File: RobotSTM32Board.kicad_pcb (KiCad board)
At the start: 2 copper layers, 70 x 82.5 mm, 74 parts, among them IC1 TB6612FNG, IC2 TB6612FNG, J1 MotorA, J10 Qwiik1, J11 Qwiik2, J12 Qwiik3, J13 Qwiik4, J14 Qwiik5, J2 MotorB, J3 MotorC, J4 MotorD, J5 EncoderA, J6 EncoderB, J7 EncoderC, J8 EncoderD, J9 ESTOP, Q1 NPN, Q2 NMOS_Substrate, Q3 NMOS_Substrate, U1 NUCLEO-F411RE, U3 TPS564252DRLR, U4 TPS51386RJNR, U5 LM27403SQ/NOPB

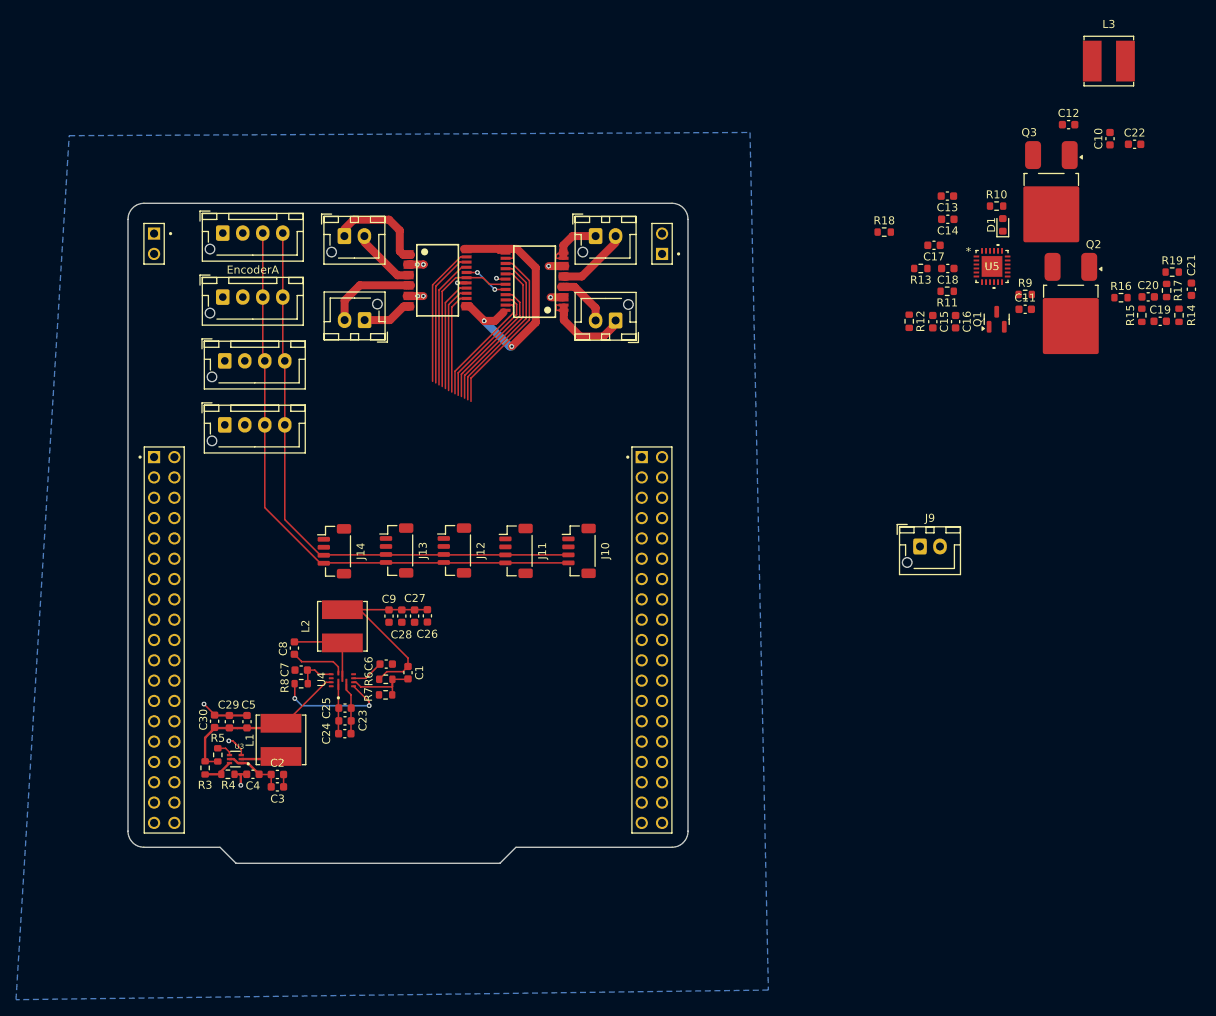
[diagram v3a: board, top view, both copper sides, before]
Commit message: pcb routed
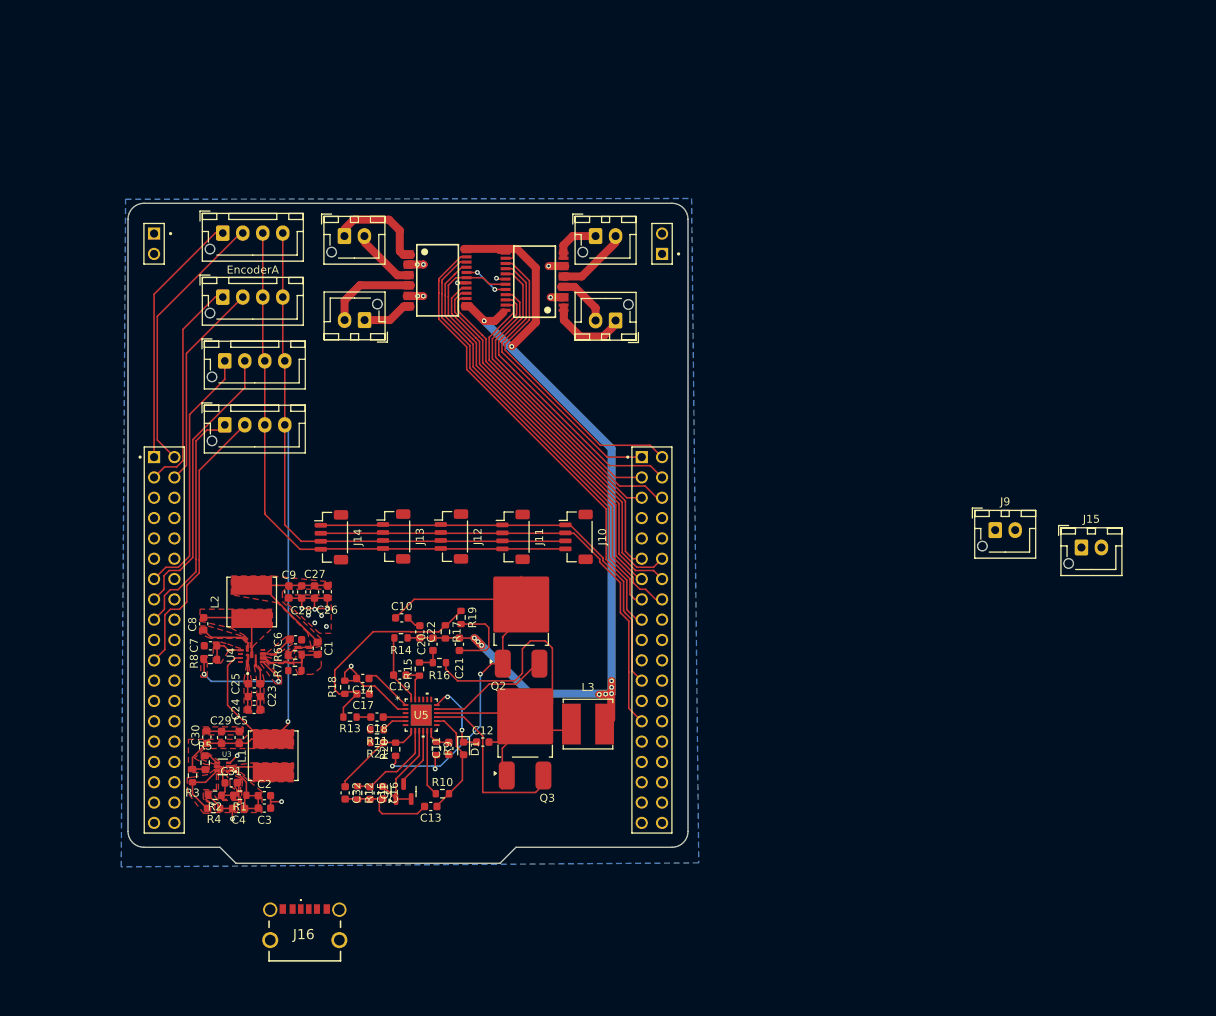
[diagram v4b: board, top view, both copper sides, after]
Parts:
- added ?: , , B.Cu at (145.2, 116.2)
- added C31: 10nF, Capacitor_SMD:C_0603_1608Metric, F.Cu at (121.4, 124.7)
- added C32: 10nF, Capacitor_SMD:C_0603_1608Metric, F.Cu at (135.6, 125.9)
- added J15: DCIn, Connector_JST:JST_XH_B2B-XH-AM_1x02_P2.50mm_Vertical, F.Cu at (227.7, 95.3)
- added J16: UJC-H-G-SMT-2-P6-TR, USBCC:UJCHGSMT2P6TR, F.Cu at (130.6, 143.5)
- added R1: 47k, Resistor_SMD:R_0603_1608Metric, F.Cu at (122.5, 126.2)
- added R2: 20k, Resistor_SMD:R_0603_1608Metric, F.Cu at (119.4, 126.2)
- added R20: 47k, Resistor_SMD:R_0603_1608Metric, F.Cu at (141.9, 120.5)
- added R21: 20k, Resistor_SMD:R_0603_1608Metric, F.Cu at (139.6, 119.7)
- moved C22 108.2 mm to (145.0, 105.8), turned to -90 degrees
- moved C10 106.9 mm to (142.7, 104.1), turned to 0 degrees
- moved C12 106.4 mm to (152.8, 119.6)
- moved L3 105.4 mm to (166.0, 117.3)
- moved R14 105.3 mm to (142.6, 106.6), turned to 0 degrees
- moved C19 104.8 mm to (142.5, 111.2), turned to 180 degrees
- moved C21 101.7 mm to (149.9, 107.4), turned to 90 degrees
- moved R10 101.0 mm to (147.8, 126.0)
- moved R15 100.5 mm to (144.9, 110.5)
- moved C13 100.0 mm to (146.3, 127.7)
- moved R17 99.7 mm to (148.2, 105.8)
- moved C20 99.4 mm to (146.6, 107.4), turned to 90 degrees
- moved R19 98.8 mm to (150.1, 104.0), turned to -90 degrees
- moved R16 96.6 mm to (147.4, 109.7)
- moved Q1 94.8 mm to (142.9, 125.8)
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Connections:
- U1 pad CN10_1: unconnected-(U1B-PC9-PadCN10_1) -> MotorDCW
- U1 pad CN10_11: unconnected-(U1B-PA5-PadCN10_11) -> MotorPWMB
- U1 pad CN10_12: unconnected-(U1B-PA12-PadCN10_12) -> MotorBCW
- U1 pad CN10_13: unconnected-(U1B-PA6-PadCN10_13) -> ESTOP
- U1 pad CN10_14: unconnected-(U1B-PA11-PadCN10_14) -> MotorBCCW
- U1 pad CN10_15: unconnected-(U1B-PA7-PadCN10_15) -> MotorACCW
- U1 pad CN10_16: unconnected-(U1B-PB12-PadCN10_16) -> MotorACW
- U1 pad CN10_17: unconnected-(U1B-PB6-PadCN10_17) -> MotorPWMA
- U1 pad CN10_2: unconnected-(U1B-PC8-PadCN10_2) -> MotorPWMD
- U1 pad CN10_23: unconnected-(U1B-PA8-PadCN10_23) -> SCL
- U1 pad CN10_27: unconnected-(U1B-PB4-PadCN10_27) -> SDA
- U1 pad CN10_3: unconnected-(U1B-PB8-PadCN10_3) -> MotorCCW
- U1 pad CN10_4: unconnected-(U1B-PC6-PadCN10_4) -> MotorDCCW
- U1 pad CN10_5: unconnected-(U1B-PB9-PadCN10_5) -> MotorPWMC
- U1 pad CN10_6: unconnected-(U1B-PC5-PadCN10_6) -> MotorCCCW
- U1 pad CN10_9: unconnected-(U1B-GND_9-PadCN10_9) -> GND
- U1 pad CN7_1: MotorPWMA -> EncoderA1
- U1 pad CN7_13: MotorBCW -> EncoderC1
- U1 pad CN7_15: unconnected-(U1A-PA14-PadCN7_15) -> EncoderC2
- U1 pad CN7_17: unconnected-(U1A-PA15-PadCN7_17) -> EncoderD1
- U1 pad CN7_19: unconnected-(U1A-GND_19-PadCN7_19) -> GND
- U1 pad CN7_2: MotorACCW -> EncoderA2
- U1 pad CN7_21: unconnected-(U1A-PB7-PadCN7_21) -> EncoderD2
- U1 pad CN7_22: unconnected-(U1A-GND_22-PadCN7_22) -> GND
- U1 pad CN7_3: MotorACW -> EncoderB1
- U1 pad CN7_4: MotorBCCW -> EncoderB2
- U1 pad CN7_8: unconnected-(U1A-GND_8-PadCN7_8) -> GND
- U3 pad 5: Vin -> Net-(U3-EN)
- U5 pad 6: unconnected-(U5-SYNC-Pad6) -> GND
- U5 pad 7: unconnected-(U5-UVLO/EN-Pad7) -> Net-(U5-UVLO/EN)
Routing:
- net 6V: track 37.4 -> 123.3 mm, vias 2 -> 10
- net Net-(Q2-Bulk): track 0.00 -> 63.6 mm
- net SDA: track 0.00 -> 58.7 mm
- net Vin: track 13.7 -> 70.8 mm, vias 0 -> 3
- net SCL: track 0.00 -> 54.4 mm
- net GND: track 113.3 -> 160.3 mm, vias 11 -> 19
- net 3V3: track 102.5 -> 147.4 mm, vias 2 -> 3
- net MotorPWMA: track 17.7 -> 58.1 mm
- net MotorACW: track 16.5 -> 55.1 mm
- net MotorACCW: track 17.2 -> 54.8 mm
- net MotorBCCW: track 14.1 -> 49.7 mm
- net EncoderC2: track 0.00 -> 35.3 mm
- net EncoderD2: track 0.00 -> 34.8 mm
- net MotorBCW: track 13.6 -> 48.3 mm
- net ESTOP: track 20.9 -> 54.8 mm
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- added copper zone on F.Cu, net 3V3
- added copper zone on F.Cu, net 5V
- added copper zone on F.Cu, net GND
- added copper zone on F.Cu, net Net-(U3-EN)
- added copper zone on F.Cu, net Net-(U3-FB)
- added copper zone on F.Cu, net Net-(U3-PG)
- added copper zone on F.Cu, net Net-(U3-SW)
- added copper zone on F.Cu, net Net-(U4-FB)
- added copper zone on F.Cu, net Net-(U4-PG)
- added copper zone on F.Cu, net Net-(U4-SS)
- added copper zone on F.Cu, net Net-(U4-SW)
- added copper zone on F.Cu, net Net-(U4-VBST)
- added copper zone on F.Cu, net Net-(U4-VCC)
- added copper zone on F.Cu, net Vin

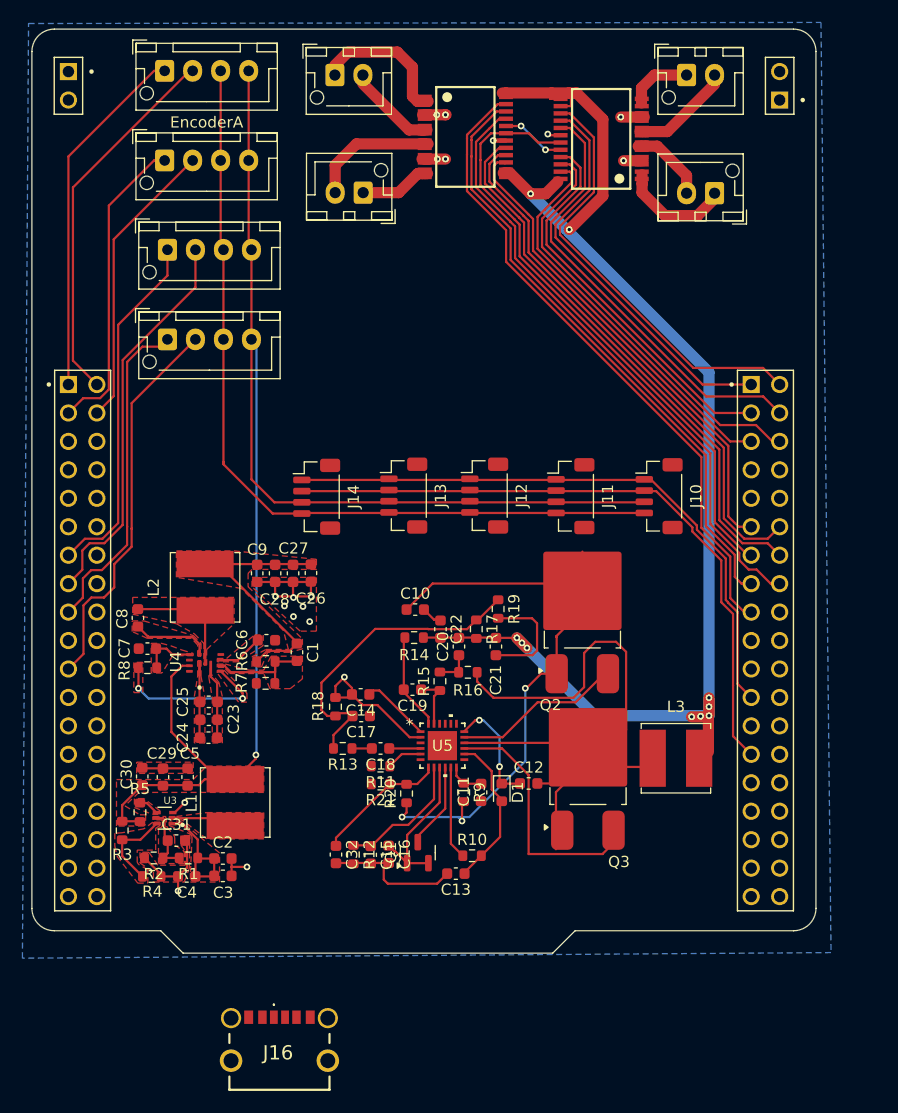
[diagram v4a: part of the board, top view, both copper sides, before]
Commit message: correcting DRC's
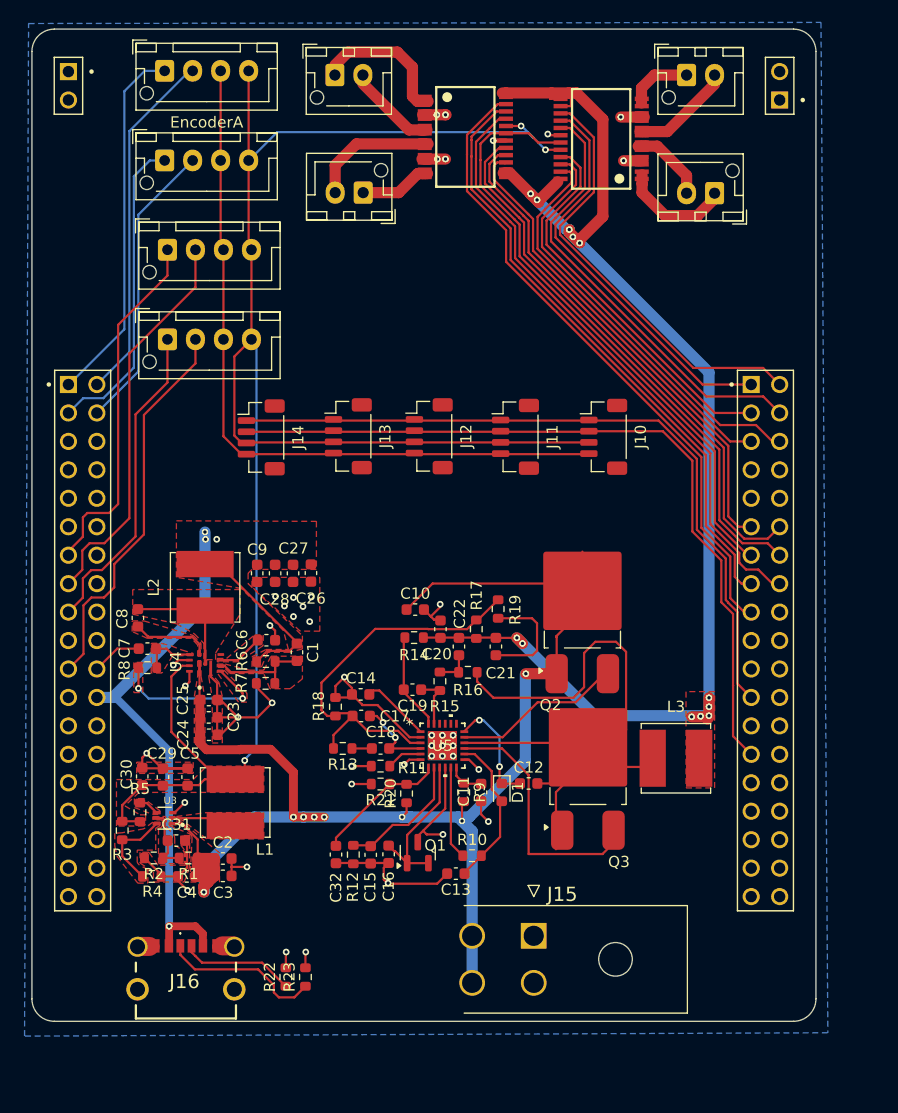
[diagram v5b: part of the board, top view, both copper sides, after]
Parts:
- added J15: 39-30-0040, KiCad:39-30-Y040, F.Cu at (153.3, 133.2)
- added R22: 20k, Resistor_SMD:R_0603_1608Metric, F.Cu at (131.2, 136.9)
- added R23: 20k, Resistor_SMD:R_0603_1608Metric, F.Cu at (132.9, 136.9)
- moved J16 10.5 mm to (122.2, 137.1)
- moved J12 7.25 mm to (144.0, 88.6)
- moved J14 7.25 mm to (129.0, 88.7)
- moved J13 7.25 mm to (136.8, 88.6)
- moved J10 7.25 mm to (159.6, 88.7)
- moved J11 7.25 mm to (151.7, 88.7)
- moved C24 0.27 mm to (124.3, 115.2)
- moved C23 0.21 mm to (124.3, 113.7)
- moved C25 0.16 mm to (124.3, 112.2)
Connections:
- J16 pad 1: unconnected-(J16-MH1-Pad1) -> GND
- J16 pad 2: unconnected-(J16-MH2-Pad2) -> GND
- J16 pad 3: unconnected-(J16-MH3-Pad3) -> GND
- J16 pad 4: unconnected-(J16-MH4-Pad4) -> GND
- J16 pad A12: unconnected-(J16-GND_1-PadA12) -> GND
- J16 pad A5: unconnected-(J16-CC1-PadA5) -> Net-(J16-CC1)
- J16 pad A9: unconnected-(J16-VBUS_1-PadA9) -> 5V
- J16 pad B12: unconnected-(J16-GND_2-PadB12) -> GND
- J16 pad B5: unconnected-(J16-CC2-PadB5) -> Net-(J16-CC2)
- J16 pad B9: unconnected-(J16-VBUS_2-PadB9) -> 5V
- U1 pad CN7_24: unconnected-(U1A-VIN-PadCN7_24) -> 5V
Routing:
- net Vin: track 70.8 -> 136.0 mm, vias 3 -> 8
- net 5V: track 25.0 -> 65.5 mm, vias 0 -> 4
- net GND: track 160.3 -> 186.5 mm, vias 19 -> 44
- net 3V3: track 147.4 -> 166.9 mm
- net Net-(J16-CC1): track 0.00 -> 14.3 mm
- net SDA: track 58.7 -> 69.3 mm
- net SCL: track 54.4 -> 64.9 mm
- net Net-(J16-CC2): track 0.00 -> 10.2 mm
- net Net-(U5-FB): track 28.1 -> 35.2 mm
- net Net-(U5-COMP): track 2.80 -> 7.22 mm, vias 0 -> 2
- net EncoderA2: track 33.5 -> 31.7 mm
- net EncoderD1: track 29.5 -> 28.6 mm
- net EncoderA1: track 32.1 -> 32.6 mm
- net 6V: track 123.3 -> 122.9 mm, vias 10 -> 12
- added copper zone on F.Cu, net 6V
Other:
- board size 70 x 82.5 mm -> 70 x 88.6 mm

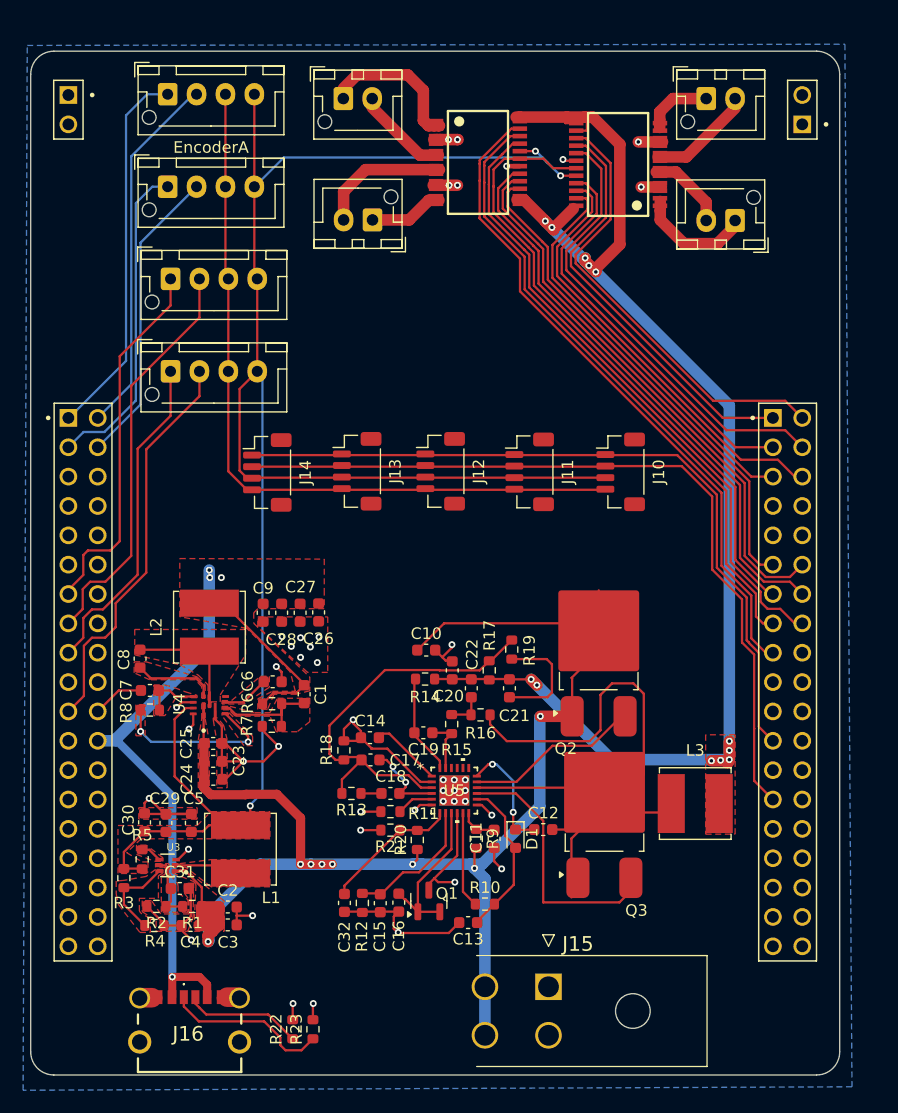
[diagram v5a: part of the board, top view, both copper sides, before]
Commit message: drc's resolved
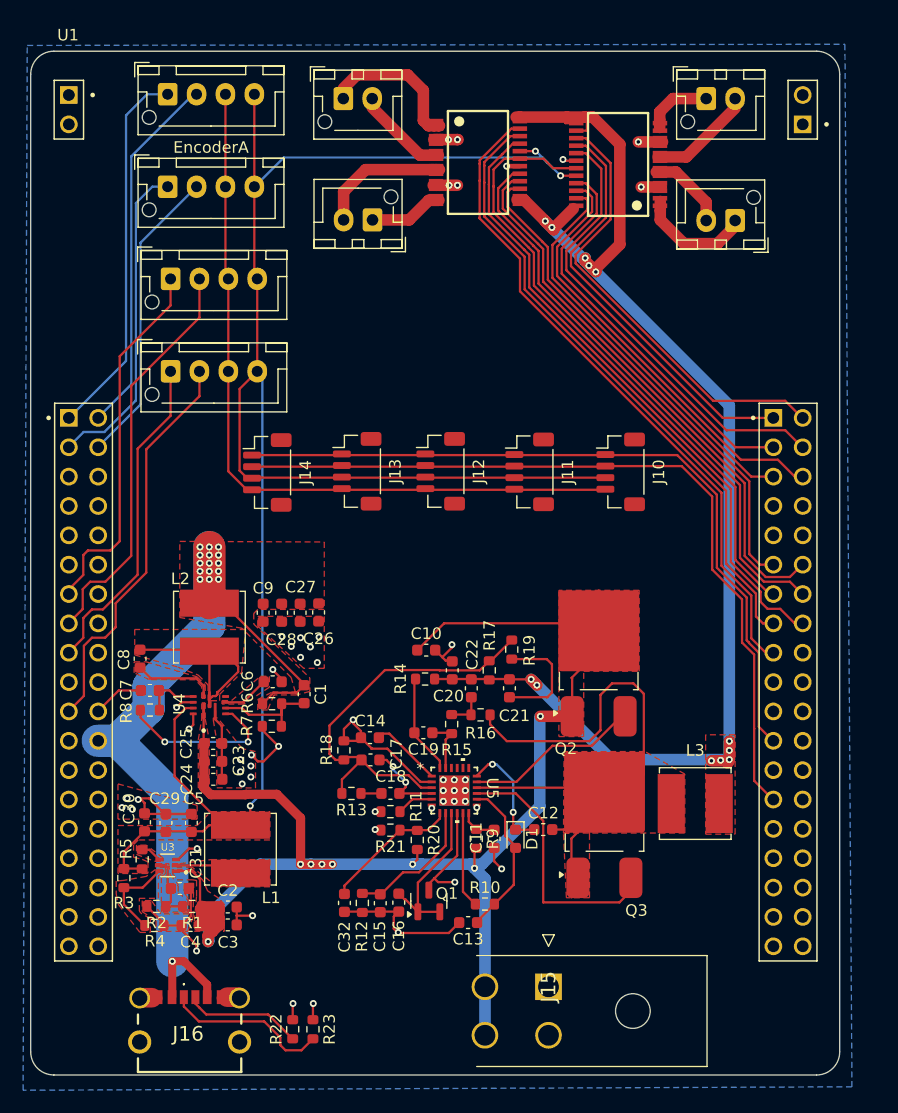
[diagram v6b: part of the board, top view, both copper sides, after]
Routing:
- net GND: track 186.5 -> 176.5 mm, vias 44 -> 52
- net 5V: track 65.5 -> 72.7 mm, vias 4 -> 16
- net Net-(U4-SW): track 10.2 -> 17.3 mm
- net Net-(Q2-Bulk): track 63.6 -> 60.1 mm
- added copper zone on F.Cu, net Net-(Q2-Bulk)
- removed copper zone on F.Cu, net Net-(U4-FB)
- removed copper zone on F.Cu, net Net-(U4-PG)
- removed copper zone on F.Cu, net Net-(U4-VCC)
